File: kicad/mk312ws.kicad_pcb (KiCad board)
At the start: 2 copper layers, 33 x 35.6 mm, 14 parts, among them J1 Conn_01x06_Male, Q1 BSS138, Q2 BSS138, Q3 BSS138, Q4 BSS138, U1 mini_esp32

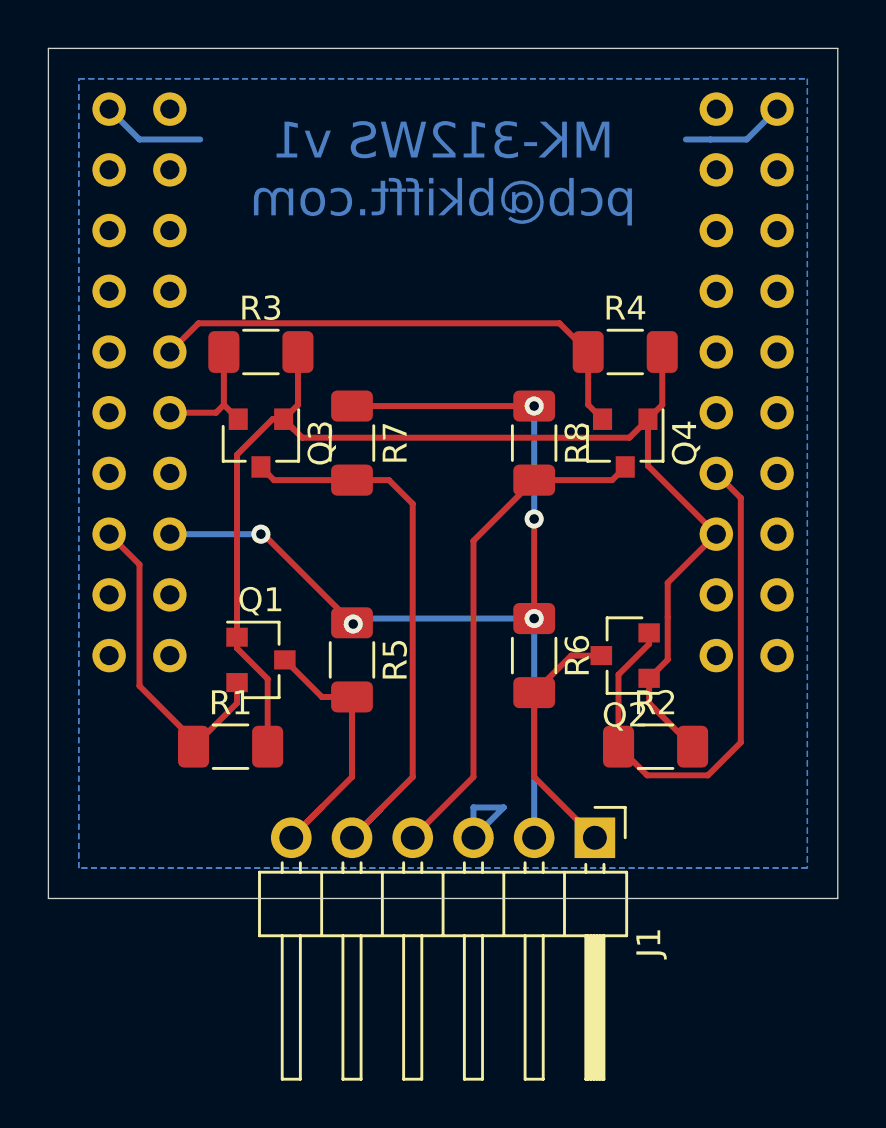
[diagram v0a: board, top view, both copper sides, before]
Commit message: adapter v2. größere pads und jumper für serial 1 loopback
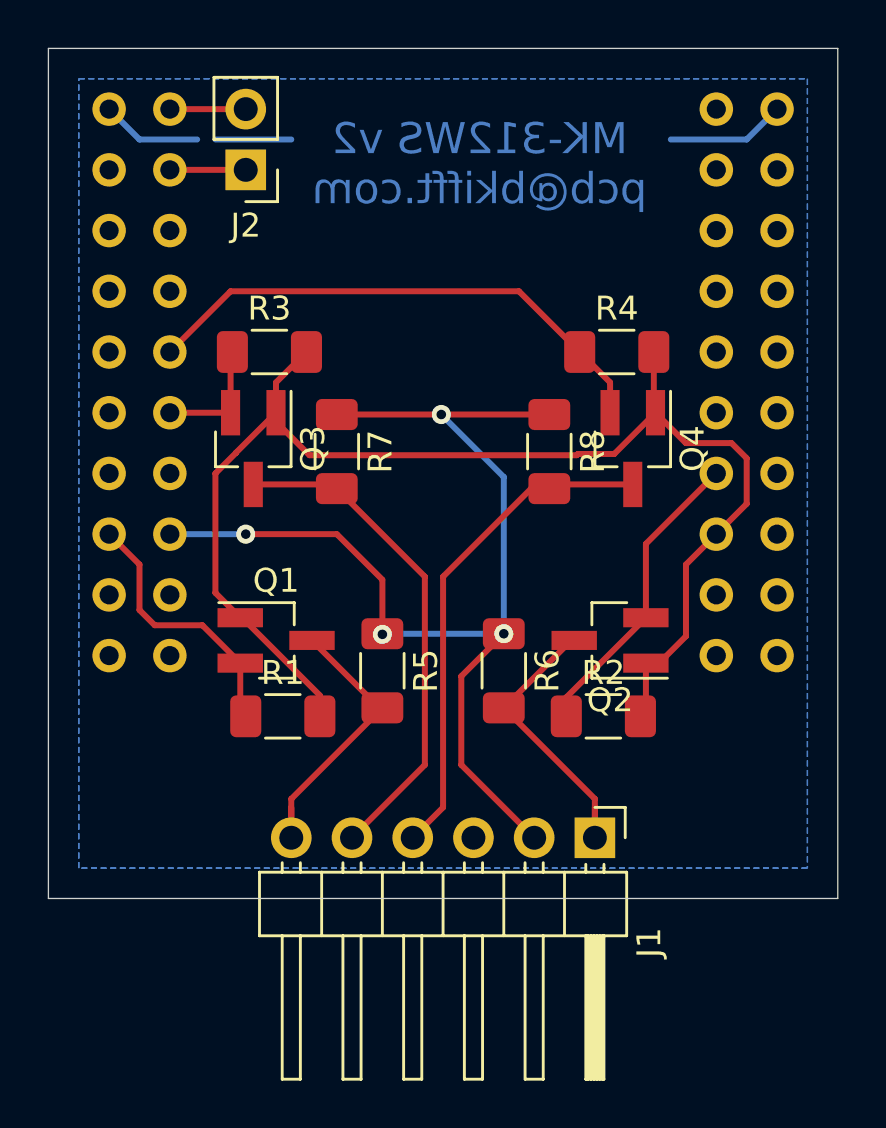
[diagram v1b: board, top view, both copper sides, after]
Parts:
- added J2: Conn_01x02_Male, Connector_PinHeader_2.54mm:PinHeader_1x02_P2.54mm_Vertical, F.Cu at (146.7, 62.2)
- Q1, Q2, Q3, Q4: footprint Package_TO_SOT_SMD:SOT-23 -> Package_TO_SOT_SMD:SOT-23_Handsoldering
- moved R1 2.53 mm to (148.2, 85.1)
- moved R2 2.53 mm to (161.6, 85.1)
- moved R6 1.42 mm to (157.5, 83.2)
- moved R5 1.35 mm to (152.4, 83.2)
- moved Q1 1.03 mm to (148.0, 81.9)
- moved Q2 0.90 mm to (161.9, 81.9)
- moved R7 0.73 mm to (150.5, 74.0)
- moved R8 0.73 mm to (159.4, 74.0)
- moved Q3 0.39 mm to (147.0, 73.9)
- moved Q4 0.39 mm to (162.9, 73.9)
- moved R3 0.36 mm to (147.7, 69.8)
- moved R4 0.35 mm to (162.2, 69.8)
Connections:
- U1 pad 21: Net-(U1-Pad21) -> DEBUG_TXD
- U1 pad 23: Net-(U1-Pad23) -> DEBUG_RXD
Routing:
- net EN_3V3: track 23.2 -> 12.8 mm
- net 5V: track 43.2 -> 46.9 mm, vias 5 -> 4
- net DEBUG_TXD: track 0.00 -> 3.18 mm
- net DEBUG_RXD: track 0.00 -> 3.18 mm
- net STATE_3V3: track 13.8 -> 11.2 mm
- net EN_Vout: track 10.6 -> 13.2 mm
- net RXD_Vout: track 23.7 -> 21.3 mm
- net 3V3: track 54.7 -> 57.0 mm
- net STATE_Vout: track 12.2 -> 13.2 mm
- net TXD_3V3: track 21.6 -> 22.3 mm
- net GND: track 13.0 -> 12.4 mm
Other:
- rule via_min_drill: 0.3 -> 0.2
- board text added: "MK-312WS v2 pcb@bkifft.com"
- board text removed: "MK-312WS v1 pcb@bkifft.com"

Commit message: kann ja keiner ahnen, dass io2 beim blitz niedrig sein muss
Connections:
- U1 pad 34: Net-(U1-Pad34) -> STATE_3V3
- U1 pad 36: STATE_3V3 -> Net-(U1-Pad36)
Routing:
- net STATE_3V3: track 11.2 -> 13.7 mm
- net GND: track 12.4 -> 13.0 mm
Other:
- board text added: "MK-312WS v3 pcb@bkifft.com"
- board text removed: "MK-312WS v2 pcb@bkifft.com"

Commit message: v3 mehr dinge. mehr fluten, mehr ausrichten
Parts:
- removed J2: Conn_01x02_Male, Connector_PinHeader_2.54mm:PinHeader_1x02_P2.54mm_Vertical
- moved Q4 17.4 mm to (147.3, 66.0), turned to 0 degrees
- moved R4 15.1 mm to (147.1, 69.1)
- moved R2 12.0 mm to (162.8, 73.2), turned to 180 degrees
- moved R8 10.3 mm to (151.4, 67.6), turned to 90 degrees
- moved R6 8.60 mm to (158.5, 74.7)
- moved R3 6.88 mm to (147.1, 76.7)
- moved Q2 5.75 mm to (162.6, 76.2)
- moved R7 1.49 mm to (151.4, 75.2), turned to 90 degrees
- moved R1 1.37 mm to (147.1, 84.3)
- moved R5 1.08 mm to (151.4, 82.8), turned to 90 degrees
- moved Q1 0.90 mm to (147.3, 81.3)
- moved Q3 0.39 mm to (147.3, 73.7), turned to 0 degrees
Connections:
- U1 pad 21: DEBUG_TXD -> Net-(U1-Pad21)
- U1 pad 23: DEBUG_RXD -> Net-(U1-Pad23)
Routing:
- net TXD_3V3: track 22.3 -> 4.56 mm
- net GND: track 13.0 -> 26.9 mm, vias 0 -> 13
- net TXD_Vout: track 21.6 -> 30.9 mm
- net EN_3V3: track 12.8 -> 4.67 mm
- net 3V3: track 57.0 -> 49.0 mm, vias 0 -> 8
- net 5V: track 46.9 -> 51.8 mm
- net EN_Vout: track 13.2 -> 16.6 mm
- net DEBUG_TXD: track 3.18 -> 0.00 mm
- net DEBUG_RXD: track 3.18 -> 0.00 mm
- net RXD_Vout: track 21.3 -> 23.1 mm
- net STATE_3V3: track 13.7 -> 12.6 mm
- net STATE_Vout: track 13.2 -> 12.4 mm
- added copper zone on F.Cu, net GND

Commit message: -.,
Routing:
- net TXD_Vout: track 30.9 -> 29.1 mm
- net GND: vias 13 -> 15
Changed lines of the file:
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@@
     (thickness 1.6)
     (drawings 5)
-    (tracks 121)
+    (tracks 124)
     (zones 0)
     (modules 14)
@@
   (segment (start 142.195001 60.915001) (end 144.989001 60.915001) (width 0.25) (layer B.Cu) (net 1))
   (segment (start 140.97 59.69) (end 142.195001 60.915001) (width 0.25) (layer B.Cu) (net 1))
+  (via (at 154.178 75.184) (size 0.8) (drill 0.4) (layers F.Cu B.Cu) (net 1))
+  (via (at 154.686 84.836) (size 0.8) (drill 0.4) (layers F.Cu B.Cu) (net 1))
   (via (at 151.384 76.708) (size 0.8) (drill 0.4) (layers F.Cu B.Cu) (net 2))
   (via (at 151.384 84.328) (size 0.8) (drill 0.4) (layers F.Cu B.Cu) (net 2))
@@
   (segment (start 148.82 66.04) (end 151.384 66.04) (width 0.25) (layer F.Cu) (net 38))
   (segment (start 155.448 88.392) (end 153.67 90.17) (width 0.25) (layer F.Cu) (net 38))
-  (segment (start 155.448 67.056) (end 155.448 88.392) (width 0.25) (layer F.Cu) (net 38))
-  (segment (start 154.432 66.04) (end 155.448 67.056) (width 0.25) (layer F.Cu) (net 38))
-  (segment (start 151.384 66.04) (end 154.432 66.04) (width 0.25) (layer F.Cu) (net 38))
+  (segment (start 153.416 73.152) (end 155.448 75.184) (width 0.25) (layer F.Cu) (net 38))
+  (segment (start 153.416 68.072) (end 153.416 73.152) (width 0.25) (layer F.Cu) (net 38))
+  (segment (start 151.384 66.04) (end 153.416 68.072) (width 0.25) (layer F.Cu) (net 38))
+  (segment (start 155.448 75.184) (end 155.448 88.392) (width 0.25) (layer F.Cu) (net 38))
   (segment (start 158.496 76.2) (end 161.06 76.2) (width 0.25) (layer F.Cu) (net 39))
   (segment (start 161.29 76.43) (end 161.06 76.2) (width 0.25) (layer F.Cu) (net 39))

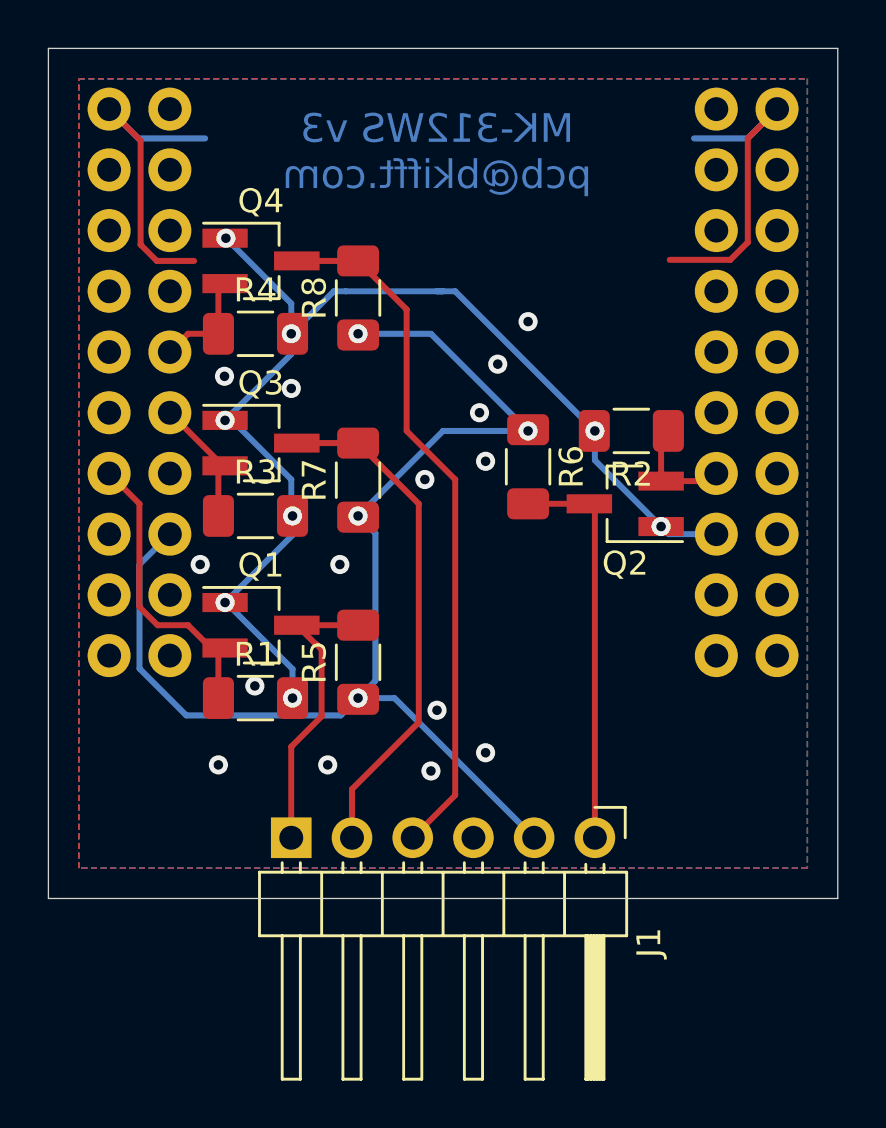
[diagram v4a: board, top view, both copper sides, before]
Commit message: v4 carrierboard. no more active components, just pins.
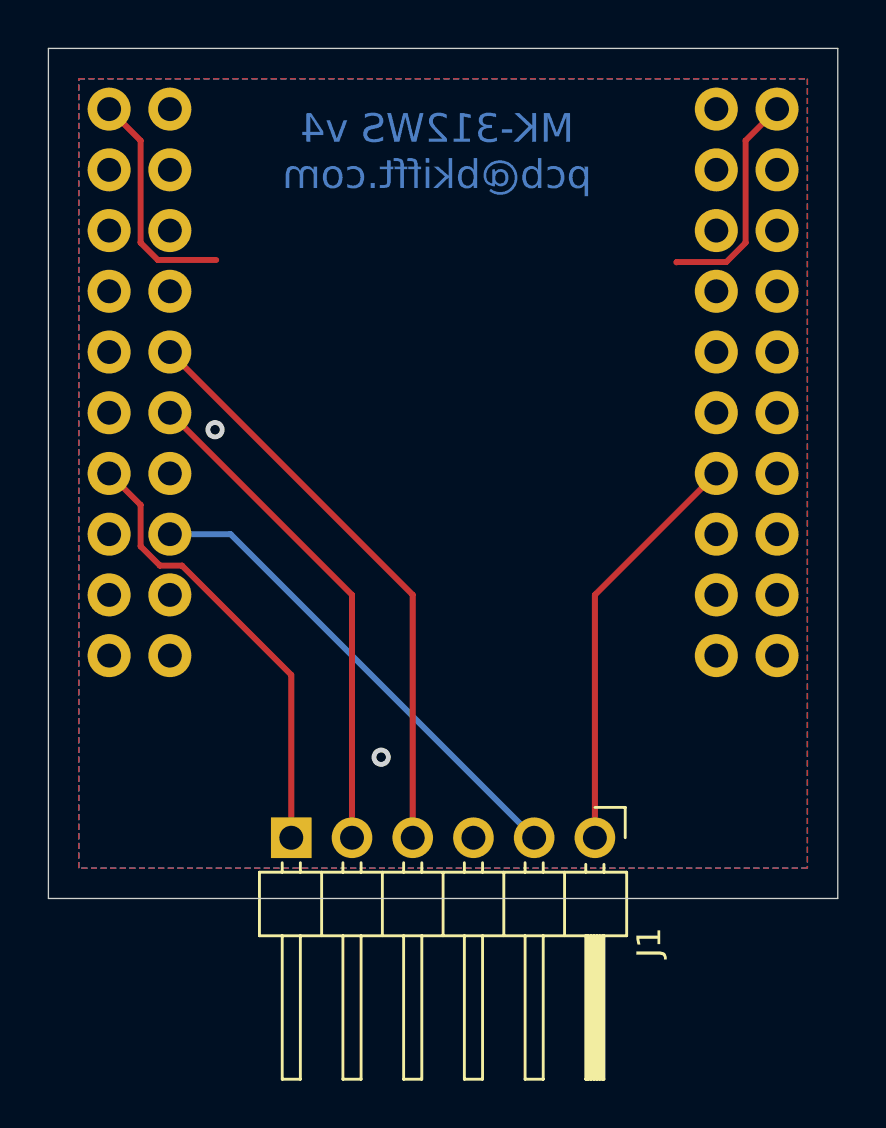
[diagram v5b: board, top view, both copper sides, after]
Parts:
- removed Q1, Q2, Q3, Q4: BSS138, Package_TO_SOT_SMD:SOT-23_Handsoldering
- removed R1, R2, R3, R4, R5, R6, R7, R8: 10K, Resistor_SMD:R_1206_3216Metric_Pad1.30x1.75mm_HandSolder
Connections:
- J1 pad 1: EN_Vout -> EN_3V3
- J1 pad 4: TXD_Vout -> TXD_3V3
- J1 pad 5: RXD_Vout -> RXD_3V3
- J1 pad 6: STATE_Vout -> STATE_3V3
- U1 pad 10: Net-(U1-Pad10) -> unconnected-(U1-Pad10)
- U1 pad 11: Net-(U1-Pad11) -> unconnected-(U1-Pad11)
- U1 pad 12: Net-(U1-Pad12) -> unconnected-(U1-Pad12)
- U1 pad 13: Net-(U1-Pad13) -> unconnected-(U1-Pad13)
- U1 pad 15: Net-(U1-Pad15) -> unconnected-(U1-Pad15)
- U1 pad 16: 3V3 -> unconnected-(U1-Pad16)
- U1 pad 17: Net-(U1-Pad17) -> unconnected-(U1-Pad17)
- U1 pad 18: Net-(U1-Pad18) -> unconnected-(U1-Pad18)
- U1 pad 19: Net-(U1-Pad19) -> unconnected-(U1-Pad19)
- U1 pad 2: Net-(U1-Pad2) -> unconnected-(U1-Pad2)
- U1 pad 20: Net-(U1-Pad20) -> unconnected-(U1-Pad20)
- U1 pad 21: Net-(U1-Pad21) -> unconnected-(U1-Pad21)
- U1 pad 23: Net-(U1-Pad23) -> unconnected-(U1-Pad23)
- U1 pad 24: Net-(U1-Pad24) -> unconnected-(U1-Pad24)
- U1 pad 25: Net-(U1-Pad25) -> unconnected-(U1-Pad25)
- U1 pad 26: Net-(U1-Pad26) -> unconnected-(U1-Pad26)
- U1 pad 27: Net-(U1-Pad27) -> unconnected-(U1-Pad27)
- U1 pad 28: Net-(U1-Pad28) -> unconnected-(U1-Pad28)
- U1 pad 3: Net-(U1-Pad3) -> unconnected-(U1-Pad3)
- U1 pad 30: Net-(U1-Pad30) -> unconnected-(U1-Pad30)
- U1 pad 32: Net-(U1-Pad32) -> unconnected-(U1-Pad32)
- U1 pad 36: Net-(U1-Pad36) -> unconnected-(U1-Pad36)
- U1 pad 37: Net-(U1-Pad37) -> unconnected-(U1-Pad37)
- U1 pad 38: Net-(U1-Pad38) -> unconnected-(U1-Pad38)
- U1 pad 39: Net-(U1-Pad39) -> unconnected-(U1-Pad39)
- U1 pad 4: Net-(U1-Pad4) -> unconnected-(U1-Pad4)
- U1 pad 40: Net-(U1-Pad40) -> unconnected-(U1-Pad40)
- U1 pad 5: Net-(U1-Pad5) -> unconnected-(U1-Pad5)
- U1 pad 6: Net-(U1-Pad6) -> unconnected-(U1-Pad6)
- U1 pad 7: Net-(U1-Pad7) -> unconnected-(U1-Pad7)
- U1 pad 8: Net-(U1-Pad8) -> unconnected-(U1-Pad8)
- U1 pad 9: Net-(U1-Pad9) -> unconnected-(U1-Pad9)
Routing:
- net 3V3: track 49.0 -> 0.00 mm, vias 8 -> 0
- net 5V: track 51.8 -> 20.5 mm, vias 4 -> 0
- net TXD_Vout: track 29.1 -> 0.00 mm
- net RXD_Vout: track 23.1 -> 0.00 mm
- net TXD_3V3: track 4.56 -> 24.5 mm
- net EN_Vout: track 16.6 -> 0.00 mm
- net RXD_3V3: track 5.44 -> 20.9 mm
- net EN_3V3: track 4.67 -> 17.3 mm
- net STATE_Vout: track 12.4 -> 0.00 mm
- net GND: track 26.9 -> 19.0 mm, vias 15 -> 2
- net STATE_3V3: track 12.6 -> 18.9 mm
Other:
- net class Default removed
- board text added: "MK-312WS v4 pcb@bkifft.com"
- board text removed: "MK-312WS v3 pcb@bkifft.com"
